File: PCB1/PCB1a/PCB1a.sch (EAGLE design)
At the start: 9 parts, among them J1 691357310006B, J2 618009231421, T1 7498011211, U8 74AHCT245, U9 74AHCT245

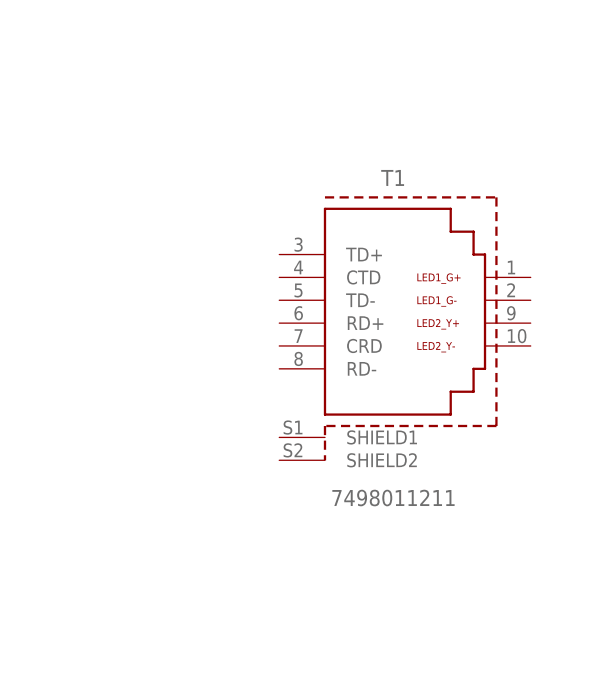
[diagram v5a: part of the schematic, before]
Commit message: ethernet remove for now.
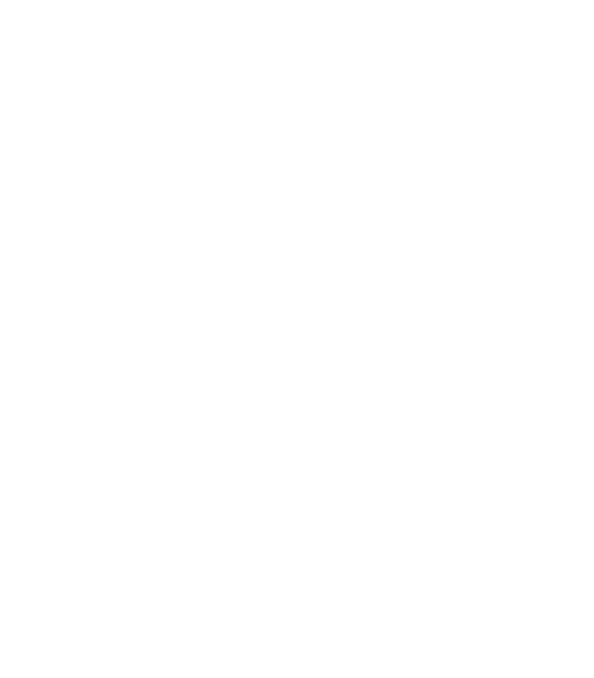
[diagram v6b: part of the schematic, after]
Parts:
- removed T1: 7498011211, Wurth_Signal & Communications_WE-RJ45_LAN:WE-RJ45_7498011211
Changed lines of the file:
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@@
 <setting verticaltext="up"/>
 </settings>
-<grid distance="0.1" unitdist="inch" unit="inch" style="lines" multiple="1" display="yes" altdistance="0.01" altunitdist="inch" altunit="inch"/>
+<grid distance="0.1" unitdist="inch" unit="inch" style="lines" multiple="1" display="no" altdistance="0.01" altunitdist="inch" altunit="inch"/>
 <layers>
 <layer number="1" name="Top" color="4" fill="1" visible="no" active="no"/>
@@
 <part name="GND19" library="supply1" library_urn="urn:adsk.eagle:library:371" deviceset="GND" device=""/>
 <part name="GND20" library="supply1" library_urn="urn:adsk.eagle:library:371" deviceset="GND" device=""/>
-<part name="T1" library="Wurth_Signal &amp; Communications_WE-RJ45_LAN" library_urn="urn:adsk.eagle:library:14284239" deviceset="WE-RJ45_7498011211" device="" package3d_urn="urn:adsk.eagle:package:12863525/4" value=" 7498011211 "/>
 </parts>
 <sheets>
@@
 <attribute name="VALUE" x="68.58" y="-93.98" size="1.778" layer="96"/>
 </instance>
-<instance part="T1" gate="G$1" x="340.36" y="-63.5" smashed="yes">
-<attribute name="NAME" x="340.36" y="-48.26" size="1.778" layer="95" align="bottom-center"/>
-<attribute name="VALUE" x="340.36" y="-83.82" size="1.778" layer="96" align="bottom-center"/>
-<attribute name="NAME" x="340.36" y="-48.26" size="1.778" layer="95" align="bottom-center"/>
-</instance>
 </instances>

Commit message: so far ...
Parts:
- added J3: ESP32_DEVC_MIN_LEFT, eclibrary:ESP32_DEVC_MIN_LEFT
- added J4: ESP32_DEVC_MIN_RIGHT, eclibrary:ESP32_DEVC_MIN_RIGHT
- added U$10, U$11, U$13, U$15, U$16, U$17, U$2, U$3, U$4, U$5, U$6, U$7, U$8, U$9: NC, eclibrary:NC
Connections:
- new net 3V3: J4.3V3
- new net N$10: J4.VP, U$9.P$1
- new net N$11: J4.34, U$10.P$1
- new net N$13: J4.EN, U$11.P$1
- new net N$14: J3.TX, U$13.P$1
- new net N$15: J3.RX, U$15.P$1
- new net N$16: J3.17, U$16.P$1
- new net N$17: J3.16, U$17.P$1
- new net N$2: J4.CMD, U$2.P$1
- new net N$3: J4.D3, U$3.P$1
- new net N$5: J4.D2, U$4.P$1
- new net N$6: J3.CLK, U$5.P$1
- new net N$7: J3.D0, U$6.P$1
- new net N$8: J3.D1, U$7.P$1
- new net N$9: J4.VN, U$8.P$1
- new net VIN: J4.5V
- net ADDRA_3V: now also J3.19
- net ADDRB_3V: now also J3.22
- net ADDRC_3V: now also J3.21
- net ADDRD_3V: now also J3.4
- net ADDRE_3V: now also J4.26
- net B1_3V: now also J4.33
- net B2_3V: now also J3.18
- net CLK_3V: now also J3.2
- net G1_3V: now also J4.14
- net G2_3V: now also J4.27
- net GND: now also J3.GND, J3.GND1, J4.GND; no longer HUB75RGB..8, HUB75RGB.8
- net LAT_3V: now also J3.15
- net M1_E: now also HUB75RGB..8, HUB75RGB.8
- net OE_3V: now also J4.13
- net R1_3V: now also J4.12
- net R2_3V: now also J4.25
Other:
- note added: "All pins marked with X are unused by SmartLED Library"
- note added: "ESP32"
- note added: "Free: Input/Analog Only"
- note added: "MatrixHardware: Hub75 Adapter Pinout, but G2 on 27"
- note added: "NC on WROVER"
- note added: "RESERVED FOR FLASH"
- note added: "RESET"
- note added: "USB Comms"

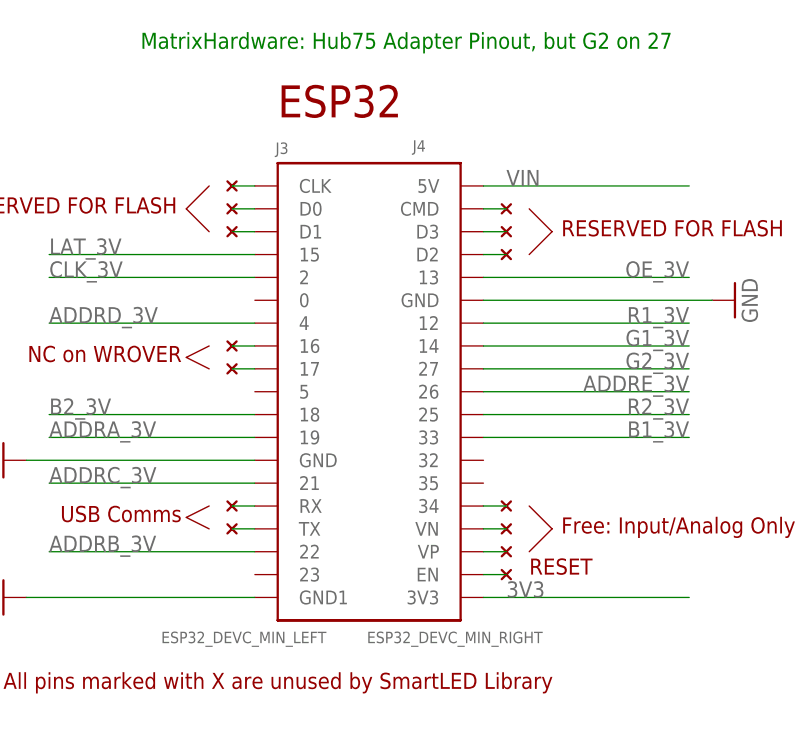
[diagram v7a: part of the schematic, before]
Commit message: ESP32 added.
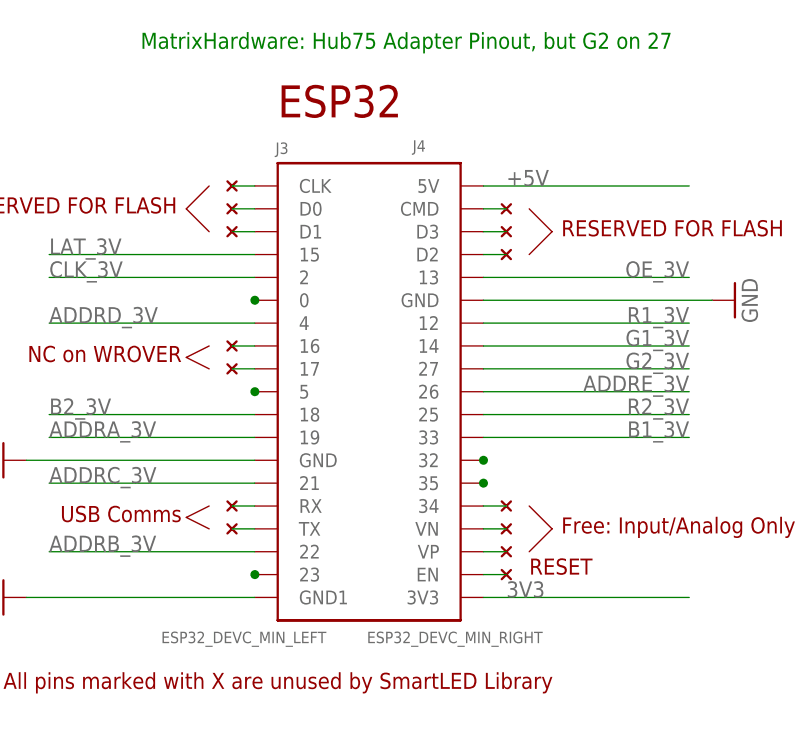
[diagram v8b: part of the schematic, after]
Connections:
- removed net VIN: J4.5V
- new net N$1: J3.0
- new net N$12: J3.23
- new net N$18: J4.35
- new net N$19: J4.32
- new net N$4: J3.5
- net +5V: now also J4.5V
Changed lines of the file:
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@@
 <wire x1="139.7" y1="154.94" x2="139.7" y2="163.83" width="0.1524" layer="91"/>
+</segment>
+<segment>
+<wire x1="269.24" y1="-43.18" x2="292.1" y2="-43.18" width="0.1524" layer="91"/>
+<label x="271.78" y="-43.18" size="1.778" layer="95"/>
+<pinref part="J4" gate="G$1" pin="5V"/>
 </segment>
 </net>
@@
 </segment>
 </net>
-<net name="VIN" class="0">
-<segment>
-<wire x1="269.24" y1="-43.18" x2="292.1" y2="-43.18" width="0.1524" layer="91"/>
-<label x="271.78" y="-43.18" size="1.778" layer="95"/>
-<pinref part="J4" gate="G$1" pin="5V"/>
-</segment>
-</net>
 <net name="3V3" class="1">
 <segment>
@@
 </segment>
 </net>
+<net name="N$1" class="0">
+<segment>
+<pinref part="J3" gate="G$1" pin="0"/>
+<junction x="243.84" y="-55.88"/>
+</segment>
+</net>
+<net name="N$4" class="0">
+<segment>
+<pinref part="J3" gate="G$1" pin="5"/>
+<junction x="243.84" y="-66.04"/>
+</segment>
+</net>
+<net name="N$12" class="0">
+<segment>
+<pinref part="J3" gate="G$1" pin="23"/>
+<junction x="243.84" y="-86.36"/>
+</segment>
+</net>
+<net name="N$18" class="0">
+<segment>
+<pinref part="J4" gate="G$1" pin="35"/>
+<junction x="269.24" y="-76.2"/>
+</segment>
+</net>
+<net name="N$19" class="0">
+<segment>
+<pinref part="J4" gate="G$1" pin="32"/>
+<junction x="269.24" y="-73.66"/>
+</segment>
+</net>
